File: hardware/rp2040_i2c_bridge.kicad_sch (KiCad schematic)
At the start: 26 parts, among them J3 Conn_01x02, Q1 BSS138, U2 RP2040, U3 W25Q128JVS, U4 BBQ10KBD, Y1 12MHz

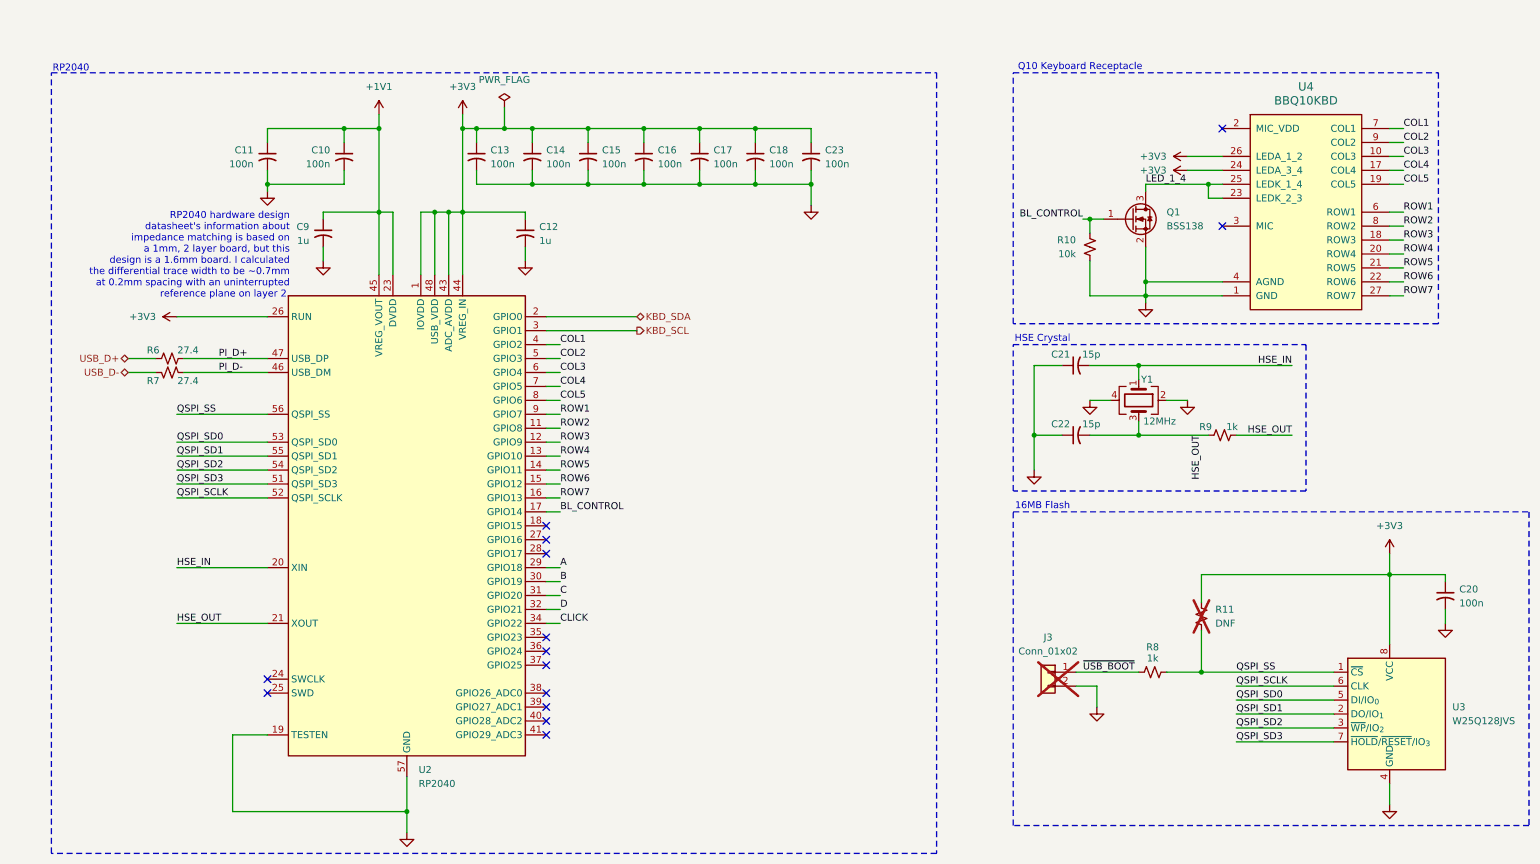
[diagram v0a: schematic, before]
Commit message: start revision to on-board SoC
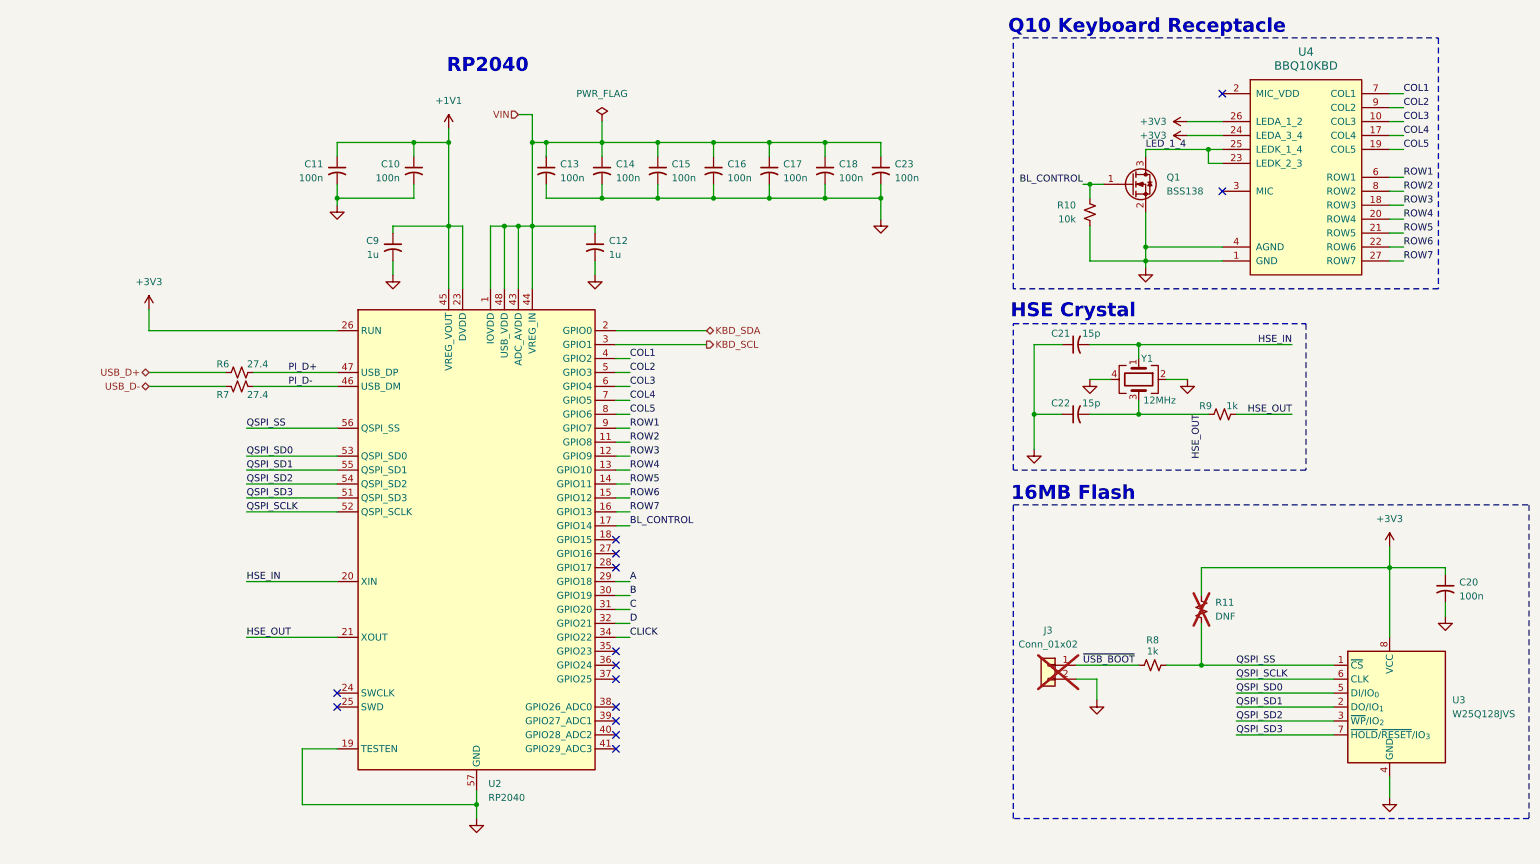
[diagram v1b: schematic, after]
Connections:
- net +3V3: no longer C12.1, C13.1, C14.1, C15.1, C16.1, C17.1, C18.1, C23.1, U2.1 (IOVDD), U2.10 (IOVDD), U2.22 (IOVDD), U2.33 (IOVDD), U2.42 (IOVDD), U2.43 (ADC_AVDD), U2.44 (VREG_IN), U2.48 (USB_VDD), U2.49 (IOVDD)
- new net VIN: C12.1, C13.1, C14.1, C15.1, C16.1, C17.1, C18.1, C23.1, U2.1 (IOVDD), U2.10 (IOVDD), U2.22 (IOVDD), U2.33 (IOVDD), U2.42 (IOVDD), U2.43 (ADC_AVDD), U2.44 (VREG_IN), U2.48 (USB_VDD), U2.49 (IOVDD)
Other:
- note removed: "RP2040 hardware design datasheet's information about impedance matching is based on a 1mm, 2 layer board, but this design is a 1.6mm board. I calculated the differential trace width to be ~0.7mm at 0.2mm spacing with an uninterrupted reference plane on layer 2."
- moved on the sheet: C10, C11, C12, C13, C14, C15, C16, C17, C18, C20, C21, C22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
